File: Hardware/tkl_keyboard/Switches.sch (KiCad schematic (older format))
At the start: 176 parts, among them SW10 K33, SW11 K49, SW12 K63, SW13 K2, SW14 K18, SW15 K34, SW16 K50, SW17 K64, SW18 K77, SW19 K3, SW2 K0, SW20 K19, SW21 K35, SW22 K51, SW23 K65, SW24 K4, SW25 K20, SW26 K36, SW27 K52, SW28 K66, SW29 K78, SW3 K16, SW30 K5, SW31 K21, SW32 K37, SW33 K53, SW34 K67, SW35 K6, SW36 K22, SW37 K38, SW38 K54, SW39 K68, SW4 K32, SW40 K79, SW41 K7, SW42 K23, SW43 K39, SW44 K55, SW45 K69, SW46 K8, SW47 K24, SW48 K40, SW49 K56, SW5 K48, SW50 K70, SW51 K80, SW52 K9, SW53 K25, SW54 K41, SW55 K57, SW56 K71, SW57 K81, SW58 K10, SW59 K26, SW6 K62, SW60 K42, SW61 K58, SW62 K72, SW63 K82, SW64 K11, SW65 K27, SW66 K43, SW67 K59, SW68 K73, SW69 K83, SW7 K76, SW70 K12, SW71 K28, SW72 K44, SW73 K60, SW74 K74, SW75 K84, SW76 K13, SW77 K29, SW78 K45, SW79 K61, SW8 K1, SW80 K85, SW81 K14, SW82 K30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

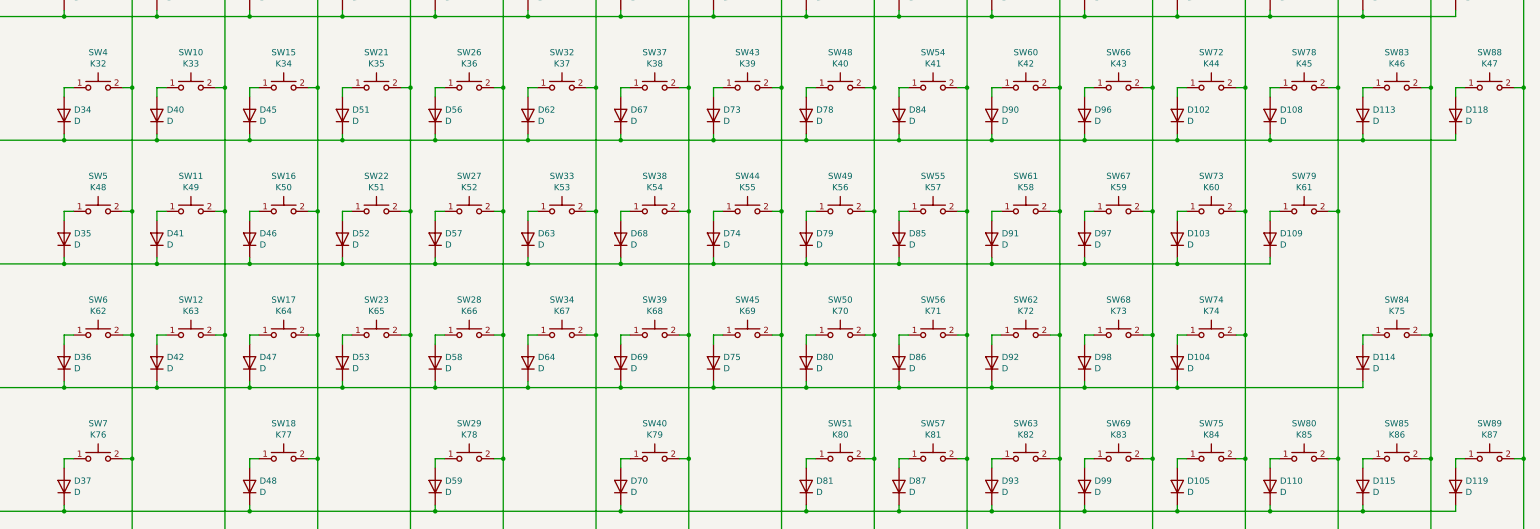
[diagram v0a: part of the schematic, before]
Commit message: Keyswitch, LED and diode placement done
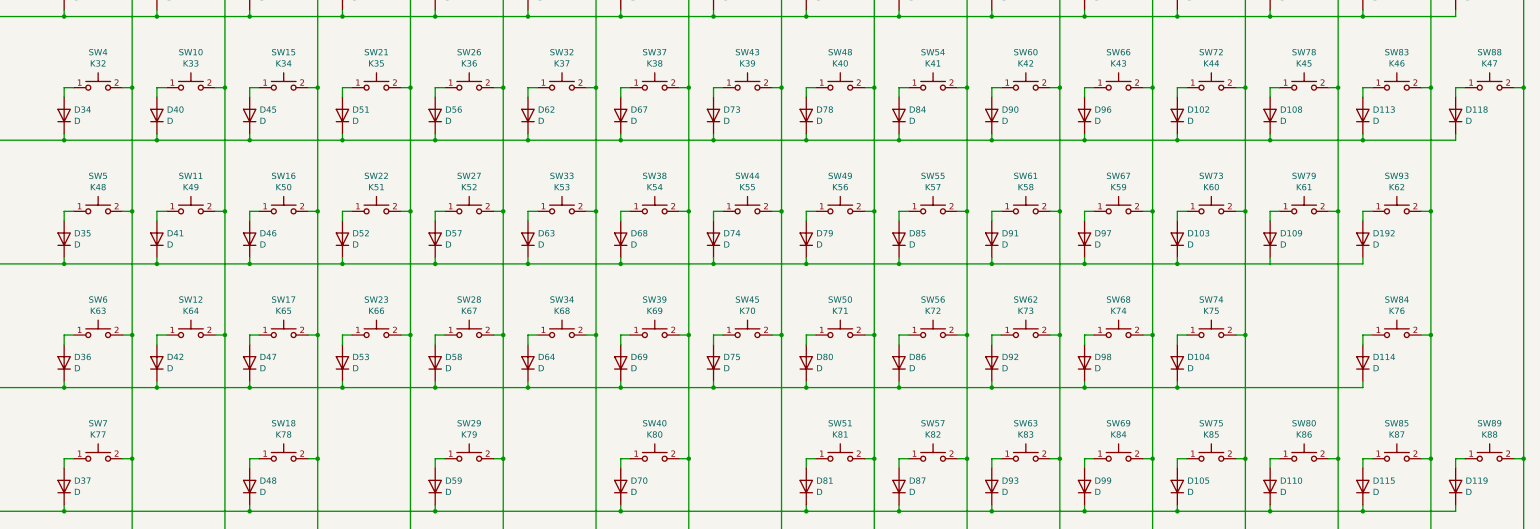
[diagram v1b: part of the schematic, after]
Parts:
- added D192: D, custom_footprint_library:SOD323_HS, symbol Device:D
- added SW93: K62, CherryMX_PCB_KailhSocket:CherryMX_1.00u_PCB_KailhSocket, symbol CherryMX:CherryMX
- SW12: value K63 -> K64; footprint CherryMX_PCB_KailhSocket:CherryMX_1.00u_PCB_KailhSocket -> CherryMX_PCB_KailhSocket:CherryMX_1.25u_PCB_KailhSocket
- SW17: value K64 -> K65
- SW18: value K77 -> K78; footprint CherryMX_PCB_KailhSocket:CherryMX_1.00u_PCB_KailhSocket -> CherryMX_PCB_KailhSocket:CherryMX_1.25u_PCB_KailhSocket
- SW23: value K65 -> K66
- SW28: value K66 -> K67
- SW29: value K78 -> K79; footprint CherryMX_PCB_KailhSocket:CherryMX_1.00u_PCB_KailhSocket -> CherryMX_PCB_KailhSocket_StabWireBottom:CherryMX_2.25u_PCB_KailhSocket_StabWireBottom
- SW34: value K67 -> K68
- SW39: value K68 -> K69
- SW4, SW78: footprint CherryMX_PCB_KailhSocket:CherryMX_1.00u_PCB_KailhSocket -> CherryMX_PCB_KailhSocket:CherryMX_1.50u_PCB_KailhSocket
- SW40: value K79 -> K80; footprint CherryMX_PCB_KailhSocket:CherryMX_1.00u_PCB_KailhSocket -> CherryMX_PCB_KailhSocket_StabWireBottom:CherryMX_6.25u_PCB_KailhSocket_StabWireBottom
- SW45: value K69 -> K70
- SW5: footprint CherryMX_PCB_KailhSocket:CherryMX_1.00u_PCB_KailhSocket -> CherryMX_PCB_KailhSocket:CherryMX_1.75u_PCB_KailhSocket
- SW50: value K70 -> K71
- SW51: value K80 -> K81; footprint CherryMX_PCB_KailhSocket:CherryMX_1.00u_PCB_KailhSocket -> CherryMX_PCB_KailhSocket_StabWireBottom:CherryMX_2.25u_PCB_KailhSocket_StabWireBottom
- SW56: value K71 -> K72
- SW57: value K81 -> K82; footprint CherryMX_PCB_KailhSocket:CherryMX_1.00u_PCB_KailhSocket -> CherryMX_PCB_KailhSocket:CherryMX_1.25u_PCB_KailhSocket
- SW6: value K62 -> K63; footprint CherryMX_PCB_KailhSocket:CherryMX_1.00u_PCB_KailhSocket -> CherryMX_PCB_KailhSocket_StabWireBottom:CherryMX_2.25u_PCB_KailhSocket_StabWireBottom
- SW62: value K72 -> K73
- SW63: value K82 -> K83; footprint CherryMX_PCB_KailhSocket:CherryMX_1.00u_PCB_KailhSocket -> CherryMX_PCB_KailhSocket:CherryMX_1.25u_PCB_KailhSocket
- SW68: value K73 -> K74
- SW69: value K83 -> K84; footprint CherryMX_PCB_KailhSocket:CherryMX_1.00u_PCB_KailhSocket -> CherryMX_PCB_KailhSocket:CherryMX_1.25u_PCB_KailhSocket
- SW7: value K76 -> K77; footprint CherryMX_PCB_KailhSocket:CherryMX_1.00u_PCB_KailhSocket -> CherryMX_PCB_KailhSocket:CherryMX_1.25u_PCB_KailhSocket
- SW73: footprint CherryMX_PCB_KailhSocket:CherryMX_1.00u_PCB_KailhSocket -> CherryMX_PCB_KailhSocket_StabWireBottom:CherryMX_2.25u_PCB_KailhSocket_StabWireBottom
- SW74: value K74 -> K75; footprint CherryMX_PCB_KailhSocket:CherryMX_1.00u_PCB_KailhSocket -> CherryMX_PCB_KailhSocket_StabWireBottom:CherryMX_2.75u_PCB_KailhSocket_StabWireBottom
- SW75: value K84 -> K85; footprint CherryMX_PCB_KailhSocket:CherryMX_1.00u_PCB_KailhSocket -> CherryMX_PCB_KailhSocket:CherryMX_1.25u_PCB_KailhSocket
- SW77: footprint CherryMX_PCB_KailhSocket:CherryMX_1.00u_PCB_KailhSocket -> CherryMX_PCB_KailhSocket_StabWireBottom:CherryMX_2.00u_PCB_KailhSocket_StabWireBottom
- SW80: value K85 -> K86
- SW84: value K75 -> K76
- SW85: value K86 -> K87
- SW89: value K87 -> K88
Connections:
- net COL[14]: now also SW93.2
- net ROW[3]: now also D192.1 (K)
- new net: D192.2 (A), SW93.1

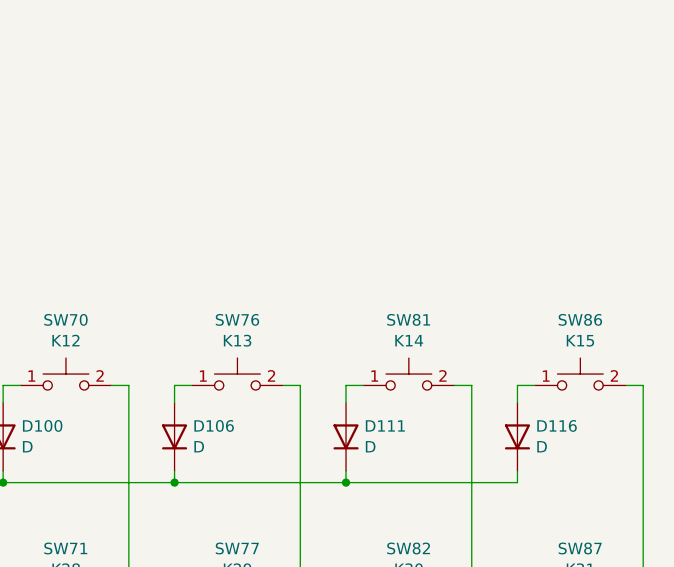
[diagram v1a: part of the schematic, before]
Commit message: LEDs and diodes routed
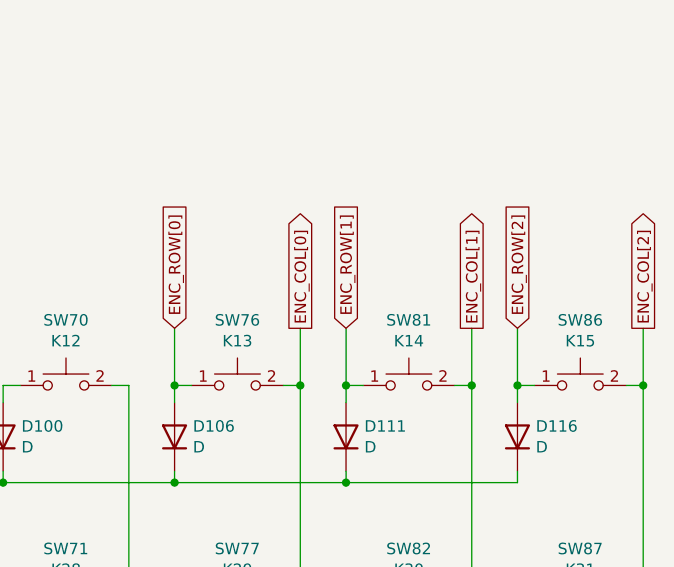
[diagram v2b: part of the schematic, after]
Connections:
- net ENC_ROW[0]: now reaches D106.2 (A), SW76.1
- net ENC_ROW[1]: now reaches D111.2 (A), SW81.1
- net ENC_ROW[2]: now reaches D116.2 (A), SW86.1
- net COL[13] renamed ENC_COL[0]
- net COL[14] renamed ENC_COL[1]
- net COL[15] renamed ENC_COL[2]
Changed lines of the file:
@@
 	1    0    0    -1
 $EndComp
+Text GLabel 12250 2250 1    50   Input ~ 0
+ENC_ROW[0]
+Text GLabel 12800 2250 1    50   Output ~ 0
+ENC_COL[0]
+Wire Wire Line
+	12250 2250 12250 2500
+Connection ~ 12250 2500
+Wire Wire Line
+	12800 2250 12800 2500
+Connection ~ 12800 2500
+Text GLabel 13000 2250 1    50   Input ~ 0
+ENC_ROW[1]
+Text GLabel 13550 2250 1    50   Output ~ 0
+ENC_COL[1]
+Wire Wire Line
+	13000 2250 13000 2500
+Wire Wire Line
+	13550 2250 13550 2500
+Connection ~ 13000 2500
+Connection ~ 13550 2500
+Text GLabel 13750 2250 1    50   Input ~ 0
+ENC_ROW[2]
+Text GLabel 14300 2250 1    50   Output ~ 0
+ENC_COL[2]
+Wire Wire Line
+	13750 2250 13750 2500
+Wire Wire Line
+	14300 2250 14300 2500
+Connection ~ 13750 2500
+Connection ~ 14300 2500
 $EndSCHEMATC

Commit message: Switch matrix routed
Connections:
- net ROW[4]: no longer D42.1 (K)
- net ROW[5]: now also D42.1 (K)
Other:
- moved on the sheet: D42, SW12
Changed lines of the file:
@@
 Connection ~ 5300 6500
 Connection ~ 4550 6500
-Connection ~ 3800 6500
 Connection ~ 3050 6500
 Wire Wire Line
@@
 Wire Wire Line
 	3725 5500 3800 5500
-Wire Wire Line
-	3800 5500 3800 6500
 Wire Wire Line
 	3050 5500 3050 6500
@@
 L Device:D D42
 U 1 1 6228001F
-P 3250 6725
+P 3250 7725
 AR Path="/62F5643B/6228001F" Ref="D42"  Part="1"
 AR Path="/63013830/6228001F" Ref="D?"  Part="1"
 AR Path="/6301FD9D/6228001F" Ref="D?"  Part="1"
-F 0 "D42" V 3296 6645 50  0000 R CNN
-F 1 "D" V 3205 6645 50  0000 R CNN
-F 2 "custom_footprint_library:SOD323_HS" H 3250 6725 50  0001 C CNN
-F 3 "~" H 3250 6725 50  0001 C CNN
-	1    3250 6725
+F 0 "D42" V 3296 7645 50  0000 R CNN
+F 1 "D" V 3205 7645 50  0000 R CNN
+F 2 "custom_footprint_library:SOD323_HS" H 3250 7725 50  0001 C CNN
+F 3 "~" H 3250 7725 50  0001 C CNN
+	1    3250 7725
 	0    -1   -1   0
 $EndComp
@@
 	4475 6500 4550 6500
 Wire Wire Line
-	3725 6500 3800 6500
+	3725 7500 3800 7500
 Wire Wire Line
 	2975 6500 3050 6500
 Connection ~ 4000 6925
-Connection ~ 3250 6925
-Wire Wire Line
-	4000 6925 3250 6925
 Wire Wire Line
 	4000 6925 4000 6875
@@
 	2500 6925 2500 6875
 Wire Wire Line
-	3250 6925 2500 6925
-Wire Wire Line
-	3250 6875 3250 6925
-Wire Wire Line
-	3250 6500 3325 6500
-Wire Wire Line
-	3250 6575 3250 6500
+	3250 7875 3250 7925
+Wire Wire Line
+	3250 7500 3325 7500
+Wire Wire Line
+	3250 7575 3250 7500
 $Comp
 L CherryMX:CherryMX SW?
 U 1 1 6227FFF4
-P 3525 6500
+P 3525 7500
 AR Path="/6227FFF4" Ref="SW?"  Part="1"
 AR Path="/60D44364/6227FFF4" Ref="SW?"  Part="1"
@@
 AR Path="/63013830/6227FFF4" Ref="SW?"  Part="1"
 AR Path="/6301FD9D/6227FFF4" Ref="SW?"  Part="1"
-F 0 "SW12" H 3525 6785 50  0000 C CNN
-F 1 "K64" H 3525 6694 50  0000 C CNN
-F 2 "CherryMX_PCB_KailhSocket:CherryMX_1.25u_PCB_KailhSocket" H 3525 6525 50  0001 C CNN
-F 3 "" H 3525 6525 50  0001 C CNN
-	1    3525 6500
+F 0 "SW12" H 3525 7785 50  0000 C CNN
+F 1 "K64" H 3525 7694 50  0000 C CNN
+F 2 "CherryMX_PCB_KailhSocket:CherryMX_1.25u_PCB_KailhSocket" H 3525 7525 50  0001 C CNN
+F 3 "" H 3525 7525 50  0001 C CNN
+	1    3525 7500
 	1    0    0    -1
 $EndComp
@@
 Wire Wire Line
 	14300 4500 14300 7500
-Wire Wire Line
-	3800 6500 3800 8500
-Wire Wire Line
-	2500 7925 4000 7925
 Wire Wire Line
 	5300 6500 5300 8500
@@
 Connection ~ 13750 2500
 Connection ~ 14300 2500
+Wire Wire Line
+	3800 5500 3800 7500
+Wire Wire Line
+	2500 6925 4000 6925
+Connection ~ 3250 7925
+Wire Wire Line
+	3250 7925 4000 7925
+Connection ~ 3800 7500
+Wire Wire Line
+	3800 7500 3800 8500
+Wire Wire Line
+	2500 7925 3250 7925
 $EndSCHEMATC

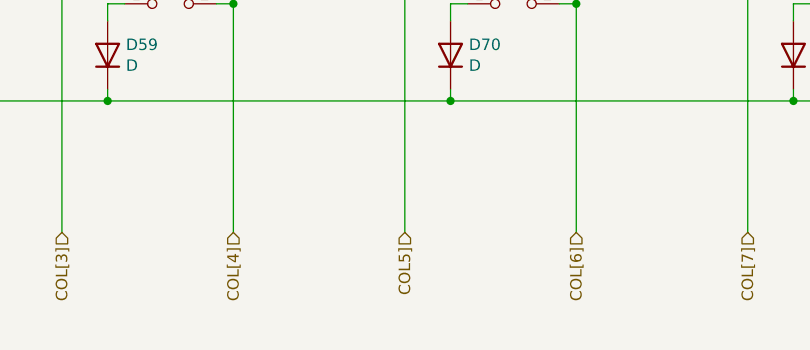
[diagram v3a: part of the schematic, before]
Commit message: Rows and columns routed to controller. Extended top board edge to fit OLED. Removed optional resistors around CMC.
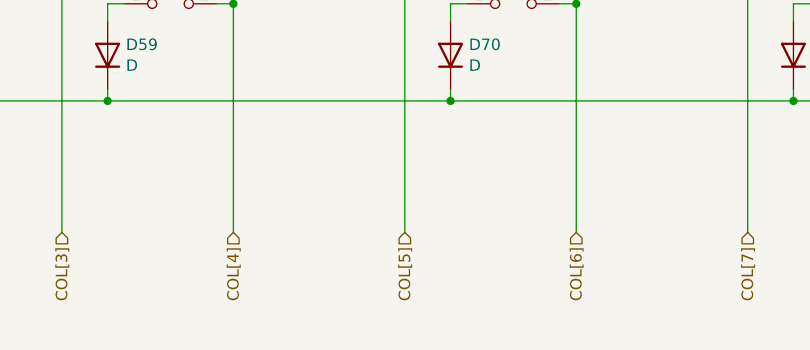
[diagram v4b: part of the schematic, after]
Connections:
- net COL5] renamed COL[5]
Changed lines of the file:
@@
 COL[4]
 Text HLabel 6800 8500 3    50   Input ~ 0
-COL5]
+COL[5]
 Text HLabel 7550 8500 3    50   Input ~ 0
 COL[6]
@@
 Wire Wire Line
 	13475 5500 13550 5500
-Wire Wire Line
-	13000 5925 12250 5925
 Wire Wire Line
 	13000 5875 13000 5925
@@
 Wire Wire Line
 	2500 7925 3250 7925
+Wire Wire Line
+	13000 5925 12250 5925
 $EndSCHEMATC

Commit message: Changing diode direction: row to column
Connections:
- net COL[0]: now also D32.1 (K), D33.1 (K), D34.1 (K), D35.1 (K), D36.1 (K), D37.1 (K); no longer SW2.2, SW3.2, SW4.2, SW5.2, SW6.2, SW7.2
- net COL[10]: now also D88.1 (K), D89.1 (K), D90.1 (K), D91.1 (K), D92.1 (K), D93.1 (K); no longer SW58.2, SW59.2, SW60.2, SW61.2, SW62.2, SW63.2
- net COL[11]: now also D94.1 (K), D95.1 (K), D96.1 (K), D97.1 (K), D98.1 (K), D99.1 (K); no longer SW64.2, SW65.2, SW66.2, SW67.2, SW68.2, SW69.2
- net COL[12]: now also D100.1 (K), D101.1 (K), D102.1 (K), D103.1 (K), D104.1 (K), D105.1 (K); no longer SW70.2, SW71.2, SW72.2, SW73.2, SW74.2, SW75.2
- net COL[1]: now also D38.1 (K), D39.1 (K), D40.1 (K), D41.1 (K), D42.1 (K); no longer SW10.2, SW11.2, SW12.2, SW8.2, SW9.2
- net COL[2]: now also D43.1 (K), D44.1 (K), D45.1 (K), D46.1 (K), D47.1 (K), D48.1 (K); no longer SW13.2, SW14.2, SW15.2, SW16.2, SW17.2, SW18.2
- net COL[3]: now also D49.1 (K), D50.1 (K), D51.1 (K), D52.1 (K), D53.1 (K); no longer SW19.2, SW20.2, SW21.2, SW22.2, SW23.2
- net COL[4]: now also D54.1 (K), D55.1 (K), D56.1 (K), D57.1 (K), D58.1 (K), D59.1 (K); no longer SW24.2, SW25.2, SW26.2, SW27.2, SW28.2, SW29.2
- net COL[5]: now also D60.1 (K), D61.1 (K), D62.1 (K), D63.1 (K), D64.1 (K); no longer SW30.2, SW31.2, SW32.2, SW33.2, SW34.2
- net COL[6]: now also D65.1 (K), D66.1 (K), D67.1 (K), D68.1 (K), D69.1 (K), D70.1 (K); no longer SW35.2, SW36.2, SW37.2, SW38.2, SW39.2, SW40.2
- net COL[7]: now also D71.1 (K), D72.1 (K), D73.1 (K), D74.1 (K), D75.1 (K); no longer SW41.2, SW42.2, SW43.2, SW44.2, SW45.2
- net COL[8]: now also D76.1 (K), D77.1 (K), D78.1 (K), D79.1 (K), D80.1 (K), D81.1 (K); no longer SW46.2, SW47.2, SW48.2, SW49.2, SW50.2, SW51.2
- net COL[9]: now also D82.1 (K), D83.1 (K), D84.1 (K), D85.1 (K), D86.1 (K), D87.1 (K); no longer SW52.2, SW53.2, SW54.2, SW55.2, SW56.2, SW57.2
- net ENC_COL[0]: now also D106.2 (A); no longer SW77.2, SW78.2, SW79.2, SW80.2
- net ENC_COL[1]: now also D111.2 (A); no longer SW82.2, SW83.2, SW84.2, SW85.2, SW93.2
- net ENC_COL[2]: now also D116.2 (A); no longer SW87.2, SW88.2, SW89.2
- net ENC_ROW[0]: now also SW13.1, SW19.1, SW2.1, SW24.1, SW30.1, SW35.1, SW41.1, SW46.1, SW52.1, SW58.1, SW64.1, SW70.1, SW8.1, SW81.1, SW86.1; no longer D106.2 (A)
- net ROW[1]: now also SW14.1, SW20.1, SW25.1, SW3.1, SW31.1, SW36.1, SW42.1, SW47.1, SW53.1, SW59.1, SW65.1, SW71.1, SW77.1, SW82.1, SW87.1, SW9.1; no longer D101.1 (K), D107.1 (K), D112.1 (K), D117.1 (K), D33.1 (K), D39.1 (K), D44.1 (K), D50.1 (K), D55.1 (K), D61.1 (K), D66.1 (K), D72.1 (K), D77.1 (K), D83.1 (K), D89.1 (K), D95.1 (K)
- net ROW[2]: now also SW10.1, SW15.1, SW21.1, SW26.1, SW32.1, SW37.1, SW4.1, SW43.1, SW48.1, SW54.1, SW60.1, SW66.1, SW72.1, SW78.1, SW83.1, SW88.1; no longer D102.1 (K), D108.1 (K), D113.1 (K), D118.1 (K), D34.1 (K), D40.1 (K), D45.1 (K), D51.1 (K), D56.1 (K), D62.1 (K), D67.1 (K), D73.1 (K), D78.1 (K), D84.1 (K), D90.1 (K), D96.1 (K)
- net ROW[3]: now also SW11.1, SW16.1, SW22.1, SW27.1, SW33.1, SW38.1, SW44.1, SW49.1, SW5.1, SW55.1, SW61.1, SW67.1, SW73.1, SW79.1, SW93.1; no longer D103.1 (K), D109.1 (K), D192.1 (K), D35.1 (K), D41.1 (K), D46.1 (K), D52.1 (K), D57.1 (K), D63.1 (K), D68.1 (K), D74.1 (K), D79.1 (K), D85.1 (K), D91.1 (K), D97.1 (K)
- net ROW[4]: now also SW17.1, SW23.1, SW28.1, SW34.1, SW39.1, SW45.1, SW50.1, SW56.1, SW6.1, SW62.1, SW68.1, SW74.1, SW84.1; no longer D104.1 (K), D114.1 (K), D36.1 (K), D47.1 (K), D53.1 (K), D58.1 (K), D64.1 (K), D69.1 (K), D75.1 (K), D80.1 (K), D86.1 (K), D92.1 (K), D98.1 (K)
- net ROW[5]: now also SW12.1, SW18.1, SW29.1, SW40.1, SW51.1, SW57.1, SW63.1, SW69.1, SW7.1, SW75.1, SW80.1, SW85.1, SW89.1; no longer D105.1 (K), D110.1 (K), D115.1 (K), D119.1 (K), D37.1 (K), D42.1 (K), D48.1 (K), D59.1 (K), D70.1 (K), D81.1 (K), D87.1 (K), D93.1 (K), D99.1 (K)
- net at D32.2 (A): now also SW2.2; no longer SW2.1
- net at D38.2 (A): now also SW8.2; no longer SW8.1
- net at D43.2 (A): now also SW13.2; no longer SW13.1
- net at D49.2 (A): now also SW19.2; no longer SW19.1
- net at D54.2 (A): now also SW24.2; no longer SW24.1
- net at D65.2 (A): now also SW35.2; no longer SW35.1
- net at D71.2 (A): now also SW41.2; no longer SW41.1
- net at D60.2 (A): now also SW30.2; no longer SW30.1
- net at D76.2 (A): now also SW46.2; no longer SW46.1
- net at D82.2 (A): now also SW52.2; no longer SW52.1
- net at D88.2 (A): now also SW58.2; no longer SW58.1
- net at D94.2 (A): now also SW64.2; no longer SW64.1
- net at D100.2 (A): now also SW70.2; no longer SW70.1
- net at D33.2 (A): now also SW3.2; no longer SW3.1
- net at D39.2 (A): now also SW9.2; no longer SW9.1
- net at D44.2 (A): now also SW14.2; no longer SW14.1
- net at D50.2 (A): now also SW20.2; no longer SW20.1
- net at D55.2 (A): now also SW25.2; no longer SW25.1
- net at D66.2 (A): now also SW36.2; no longer SW36.1
- net at D72.2 (A): now also SW42.2; no longer SW42.1
- net at D61.2 (A): now also SW31.2; no longer SW31.1
- net at D77.2 (A): now also SW47.2; no longer SW47.1
- net at D83.2 (A): now also SW53.2; no longer SW53.1
- net at D95.2 (A): now also SW65.2; no longer SW65.1
- net at D89.2 (A): now also SW59.2; no longer SW59.1
- net at D101.2 (A): now also SW71.2; no longer SW71.1
- net at D107.2 (A): now also SW77.2; no longer SW77.1
- net at D112.2 (A): now also SW82.2; no longer SW82.1
- net at D117.2 (A): now also SW87.2; no longer SW87.1
- net at D34.2 (A): now also SW4.2; no longer SW4.1
- net at D40.2 (A): now also SW10.2; no longer SW10.1
- net at D45.2 (A): now also SW15.2; no longer SW15.1
- net at D51.2 (A): now also SW21.2; no longer SW21.1
- net at D56.2 (A): now also SW26.2; no longer SW26.1
- net at D67.2 (A): now also SW37.2; no longer SW37.1
- net at D73.2 (A): now also SW43.2; no longer SW43.1
- net at D62.2 (A): now also SW32.2; no longer SW32.1
- net at D78.2 (A): now also SW48.2; no longer SW48.1
- net at D84.2 (A): now also SW54.2; no longer SW54.1
- net at D96.2 (A): now also SW66.2; no longer SW66.1
- net at D90.2 (A): now also SW60.2; no longer SW60.1
- net at D102.2 (A): now also SW72.2; no longer SW72.1
- net at D108.2 (A): now also SW78.2; no longer SW78.1
- net at D113.2 (A): now also SW83.2; no longer SW83.1
- net at D118.2 (A): now also SW88.2; no longer SW88.1
- net at D35.2 (A): now also SW5.2; no longer SW5.1
- net at D41.2 (A): now also SW11.2; no longer SW11.1
- net at D46.2 (A): now also SW16.2; no longer SW16.1
- net at D52.2 (A): now also SW22.2; no longer SW22.1
- net at D57.2 (A): now also SW27.2; no longer SW27.1
- net at D68.2 (A): now also SW38.2; no longer SW38.1
- net at D74.2 (A): now also SW44.2; no longer SW44.1
- net at D63.2 (A): now also SW33.2; no longer SW33.1
- net at D79.2 (A): now also SW49.2; no longer SW49.1
- net at D85.2 (A): now also SW55.2; no longer SW55.1
- net at D97.2 (A): now also SW67.2; no longer SW67.1
- net at D91.2 (A): now also SW61.2; no longer SW61.1
- net at D103.2 (A): now also SW73.2; no longer SW73.1
- net at D109.2 (A): now also SW79.2; no longer SW79.1
- net at D36.2 (A): now also SW6.2; no longer SW6.1
- net at D42.2 (A): now also SW12.2; no longer SW12.1
- net at D47.2 (A): now also SW17.2; no longer SW17.1
- net at D53.2 (A): now also SW23.2; no longer SW23.1
- net at D58.2 (A): now also SW28.2; no longer SW28.1
- net at D69.2 (A): now also SW39.2; no longer SW39.1
- net at D75.2 (A): now also SW45.2; no longer SW45.1
- net at D64.2 (A): now also SW34.2; no longer SW34.1
- net at D80.2 (A): now also SW50.2; no longer SW50.1
- net at D86.2 (A): now also SW56.2; no longer SW56.1
- net at D98.2 (A): now also SW68.2; no longer SW68.1
- net at D92.2 (A): now also SW62.2; no longer SW62.1
- net at D104.2 (A): now also SW74.2; no longer SW74.1
- net at D114.2 (A): now also SW84.2; no longer SW84.1
- net at D37.2 (A): now also SW7.2; no longer SW7.1
- net at D48.2 (A): now also SW18.2; no longer SW18.1
- net at D59.2 (A): now also SW29.2; no longer SW29.1
- net at D70.2 (A): now also SW40.2; no longer SW40.1
- net at D81.2 (A): now also SW51.2; no longer SW51.1
- net at D87.2 (A): now also SW57.2; no longer SW57.1
- net at D99.2 (A): now also SW69.2; no longer SW69.1
- net at D93.2 (A): now also SW63.2; no longer SW63.1
- net at D105.2 (A): now also SW75.2; no longer SW75.1
- net at D110.2 (A): now also SW80.2; no longer SW80.1
- net at D115.2 (A): now also SW85.2; no longer SW85.1
- net at D119.2 (A): now also SW89.2; no longer SW89.1
- net at D192.2 (A): now also SW93.2; no longer SW93.1
- removed net ENC_ROW[1]: D111.2 (A), SW81.1
- removed net ENC_ROW[2]: D116.2 (A), SW86.1
- removed net ROW[0]: D100.1 (K), D106.1 (K), D111.1 (K), D116.1 (K), D32.1 (K), D38.1 (K), D43.1 (K), D49.1 (K), D54.1 (K), D60.1 (K), D65.1 (K), D71.1 (K), D76.1 (K), D82.1 (K), D88.1 (K), D94.1 (K)
- new net COL[13]: D106.1 (K), D107.1 (K), D108.1 (K), D109.1 (K), D110.1 (K)
- new net COL[14]: D111.1 (K), D112.1 (K), D113.1 (K), D114.1 (K), D115.1 (K), D192.1 (K)
- new net COL[15]: D116.1 (K), D117.1 (K), D118.1 (K), D119.1 (K)
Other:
- moved on the sheet: D100, D101, D102, D103, D104, D105, D106, D107, D108, D109, D110, D111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
